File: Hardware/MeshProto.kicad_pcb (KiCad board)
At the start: 2 copper layers, 30.8 x 31.6 mm, 116 parts, among them P1 CONN_1, P10 CONN_1, P100 CONN_1, P101 CONN_1, P102 CONN_1, P103 CONN_1, P104 CONN_1, P105 CONN_1, P106 CONN_1, P107 CONN_1, P108 CONN_1, P11 CONN_1, P12 CONN_1, P13 CONN_1, P14 CONN_1, P15 CONN_1, P16 CONN_1, P17 CONN_1, P18 CONN_1, P19 CONN_1, P2 CONN_1, P20 CONN_1, P21 CONN_1, P22 CONN_1, P23 CONN_1, P24 CONN_1, P25 CONN_1, P26 CONN_1, P27 CONN_1, P28 CONN_1, P29 CONN_1, P3 CONN_1, P30 CONN_1, P31 CONN_1, P32 CONN_1, P33 CONN_1, P34 CONN_1, P35 CONN_1, P36 CONN_1, P37 CONN_1, P38 CONN_1, P39 CONN_1, P4 CONN_1, P40 CONN_1, P41 CONN_1, P42 CONN_1, P43 CONN_1, P44 CONN_1, P45 CONN_1, P46 CONN_1, P47 CONN_1, P48 CONN_1, P49 CONN_1, P5 CONN_1, P50 CONN_1, P51 CONN_1, P52 CONN_1, P53 CONN_1, P54 CONN_1, P55 CONN_1, P56 CONN_1, P57 CONN_1, P58 CONN_1, P59 CONN_1, P6 CONN_1, P60 CONN_1, P61 CONN_1, P62 CONN_1, P63 CONN_1, P64 CONN_1, P65 CONN_1, P66 CONN_1, P67 CONN_1, P68 CONN_1, P69 CONN_1, P7 CONN_1, P70 CONN_1, P71 CONN_1, P72 CONN_1, P73 CONN_1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

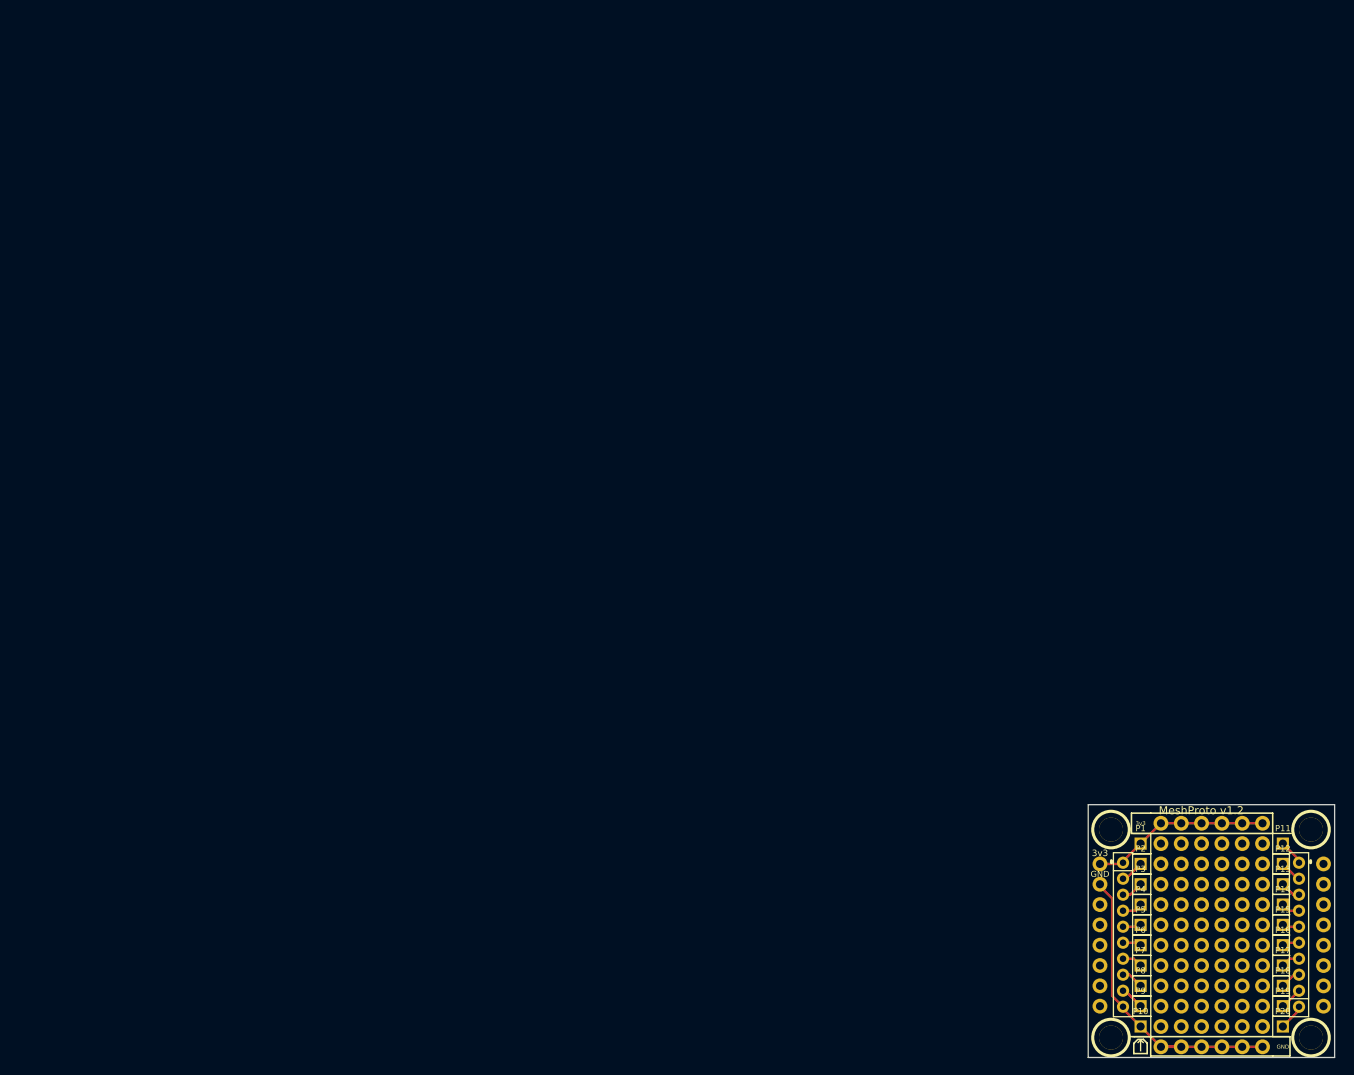
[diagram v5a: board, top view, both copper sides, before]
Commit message: Final changes, silks, logo, gerbers.
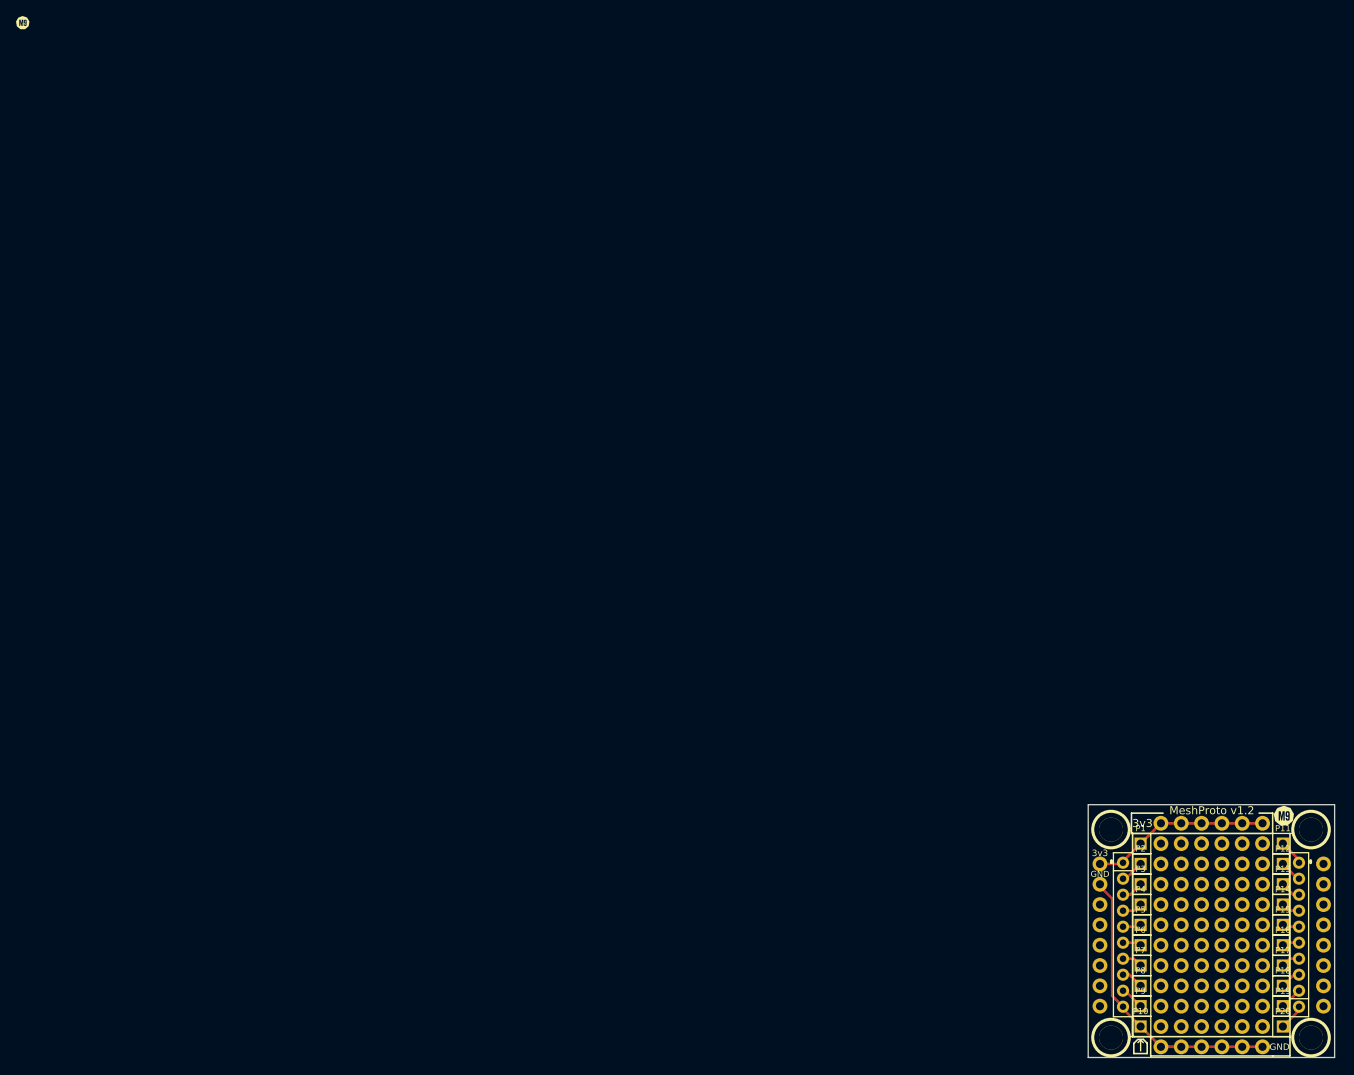
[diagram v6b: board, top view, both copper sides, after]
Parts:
- added VAL: M9Logo-2mm, _M9Logo_:M9Logo-scaled, F.Cu at (-0.01, 0.02)
- added VAL: M9Logo-2mm, _M9Logo_:M9Logo-scaled, F.Cu at (157.7, 99.1)
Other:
- board text added: "RP DC"
- board text added: "by"
